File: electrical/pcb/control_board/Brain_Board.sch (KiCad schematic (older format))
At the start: 35 parts, among them J22 S9175-ND_rpi_breakout, J23 S9175-ND_rpi_breakout, J24 6posheader, J25 SSW-104-01-F-T, J26 PEC10DAAN, J27 PPTC021LFBN-RC, J28 PPTC021LFBN-RC, J29 PPTC021LFBN-RC, M1 Mounting_Holes, Q1 2N3906, Q2 2N3906, Q3 2N3906, SW1 CT206124-ND, U6 DC7G3HWA

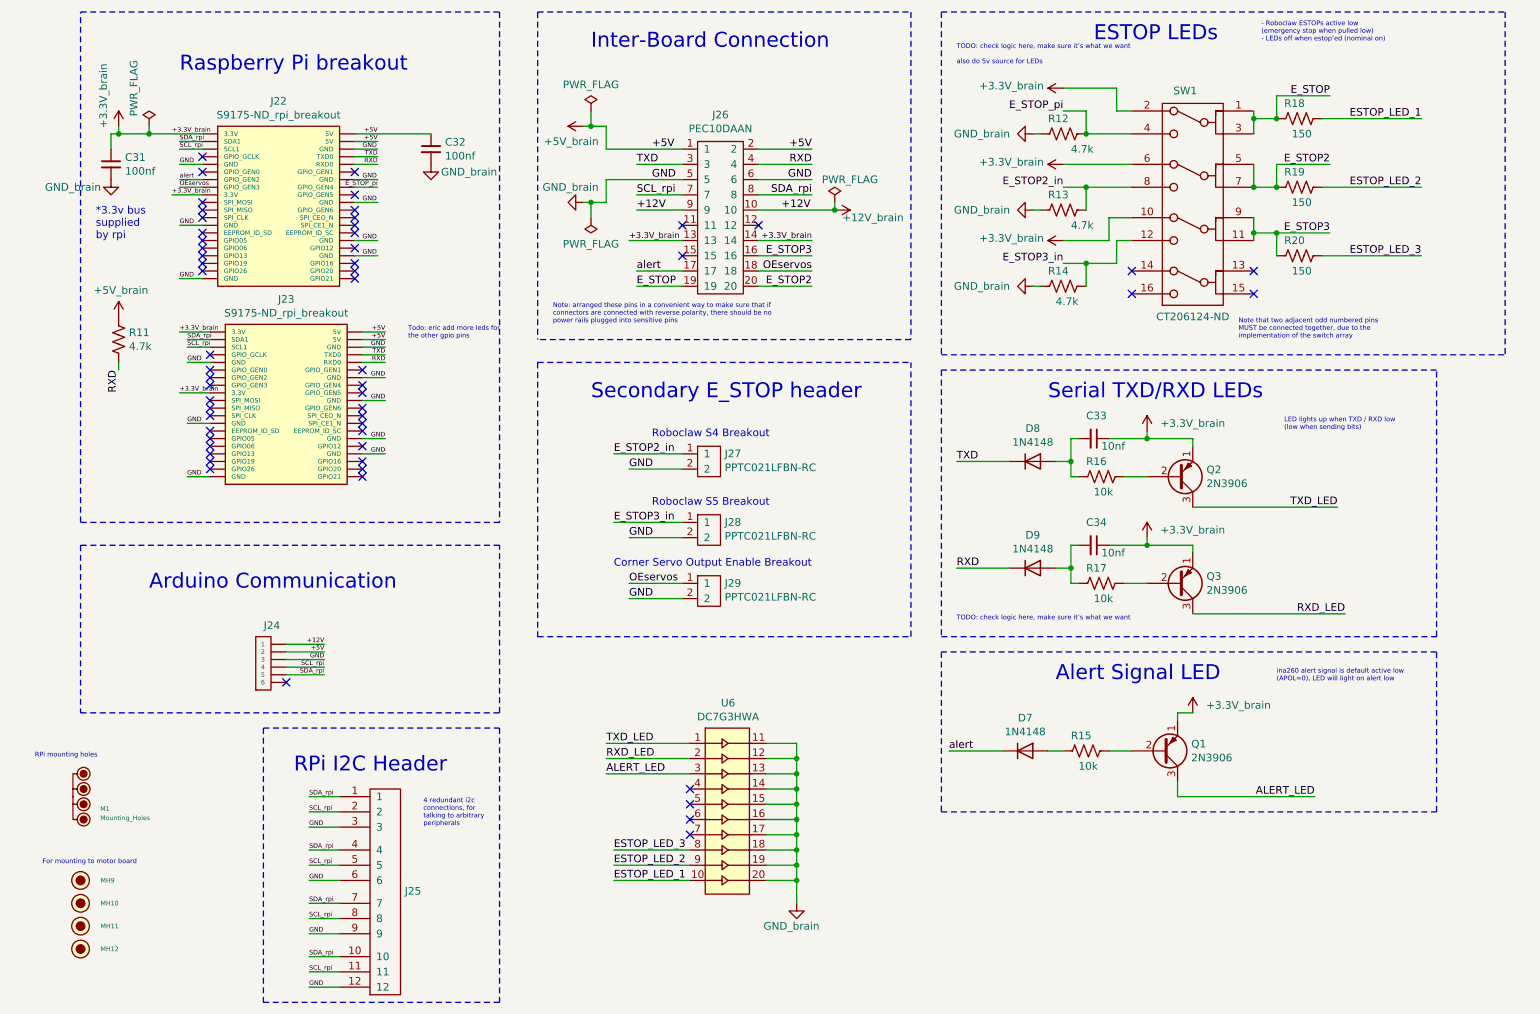
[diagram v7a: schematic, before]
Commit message: Some small updates before final routing
- Routed 12V_EN line to rpi
- A bunch of schematic cleanup
- Switched ESTOP LEDs to 5v from 3.3v
- Updated LED resistor sizing
- Connected available LEDs to unused rpi GPIOse
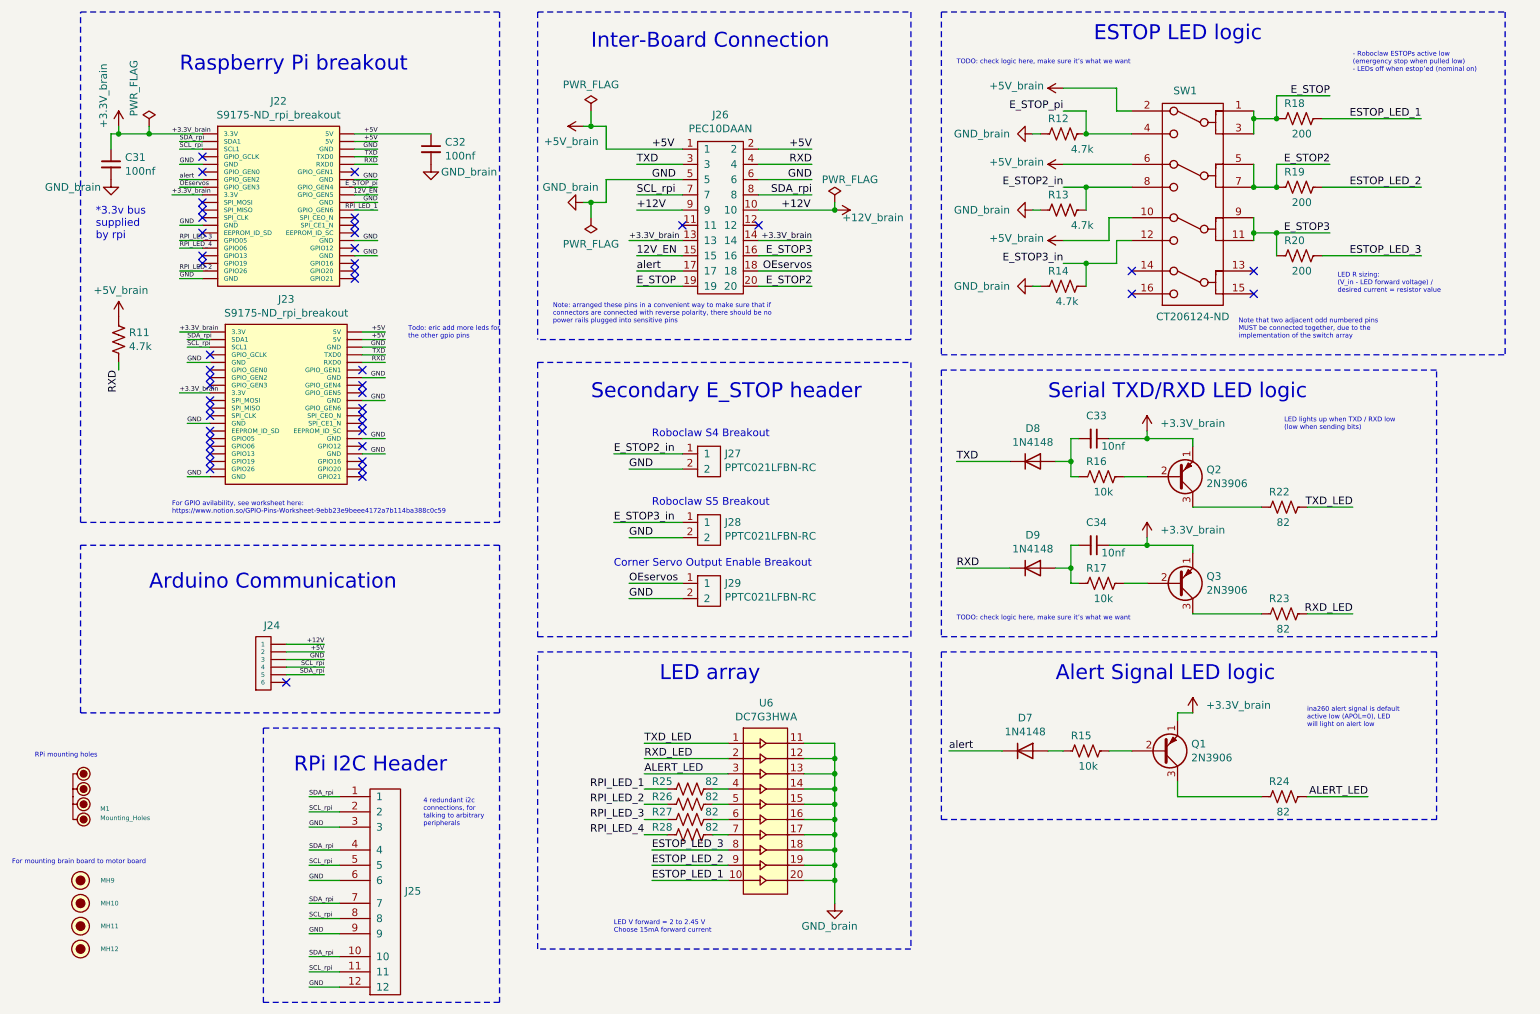
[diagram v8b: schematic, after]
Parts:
- added R22, R23, R24, R25, R26, R27, R28: 82, Resistor_THT:R_Axial_DIN0207_L6.3mm_D2.5mm_P7.62mm_Horizontal, symbol Device:R_US
- R18, R19, R20: value 150 -> 200
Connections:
- net +3.3V_brain: no longer SW1.10 (out3_1), SW1.2 (out1_1), SW1.6 (out2_1)
- net +5V_brain: now also SW1.10 (out3_1), SW1.2 (out1_1), SW1.6 (out2_1)
- net ALERT_LED: now also R24.1; no longer Q1.3 (C)
- net RXD_LED: now also R23.1; no longer Q3.3 (C)
- net TXD_LED: now also R22.1; no longer Q2.3 (C)
- net 12V_EN: now reaches J22.18 (GPIO_GEN5)
- net 12V_EN: now also J26.15
- net RPI_LED_1: now reaches J22.22 (GPIO_GEN6)
- net RPI_LED_1: now also R25.2
- net RPI_LED_3: now reaches J22.29 (GPIO05)
- net RPI_LED_3: now also R27.2
- net RPI_LED_4: now reaches J22.31 (GPIO06)
- net RPI_LED_4: now also R28.2
- net RPI_LED_2: now reaches J22.37 (GPIO26)
- net RPI_LED_2: now also R26.2
- net at U6.4: now also R25.1
- net at U6.5: now also R26.1
- net at U6.6: now also R27.1
- net at U6.7: now also R28.1
- new net: Q2.3 (C), R22.2
- new net: Q3.3 (C), R23.2
- new net: Q1.3 (C), R24.2
- no-connect marks 57 -> 47
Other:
- note added: "Alert Signal LED logic"
- note added: "ESTOP LED logic"
- note added: "For GPIO avilability, see worksheet here: \nhttps://www.notion.so/GPIO-Pins-Worksheet-9ebb23e9beee4172a7b114ba388c0c59"
- note added: "For mounting brain board to motor board"
- note added: "LED R sizing: \n(V_in - LED forward voltage) / \ndesired current = resistor value"
- note added: "LED V forward = 2 to 2.45 V\nChoose 15mA forward current"
- note added: "LED array"
- note added: "Serial TXD/RXD LED logic"
- note added: "ina260 alert signal is default \nactive low (APOL=0), LED \nwill light on alert low"
- note removed: "Alert Signal LED"
- note removed: "ESTOP LEDs"
- note removed: "For mounting to motor board"
- note removed: "Serial TXD/RXD LEDs"
- note removed: "TODO: check logic here, make sure it’s what we want\n\nalso do 5v source for LEDs"
- note removed: "ina260 alert signal is default active low \n(APOL=0), LED will light on alert low"
- moved on the sheet: U6
